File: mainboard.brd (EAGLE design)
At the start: 65 x 56 mm, 19 parts, among them J1 RASPBERRYPI-40-PIN-GPIO

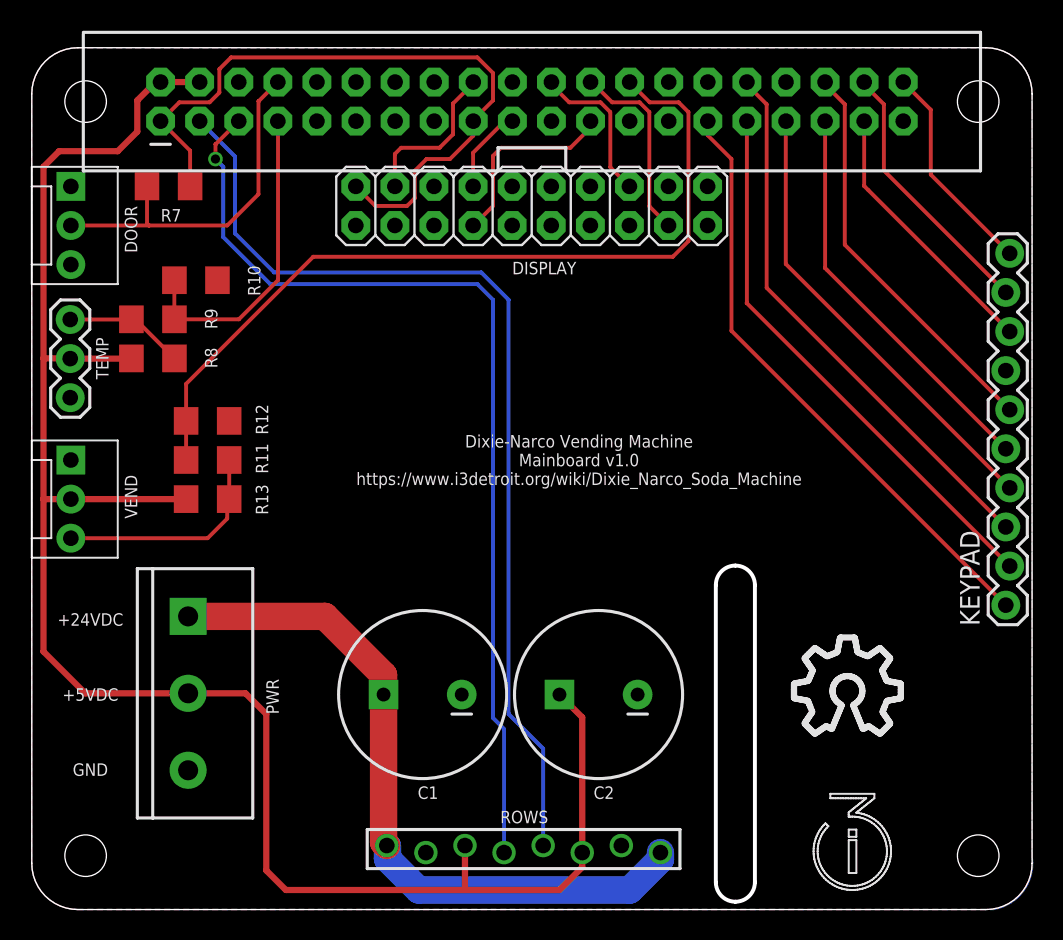
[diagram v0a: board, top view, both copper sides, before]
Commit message: Completed mainboard design edits; buffers for keypad, reworked 5V feed.
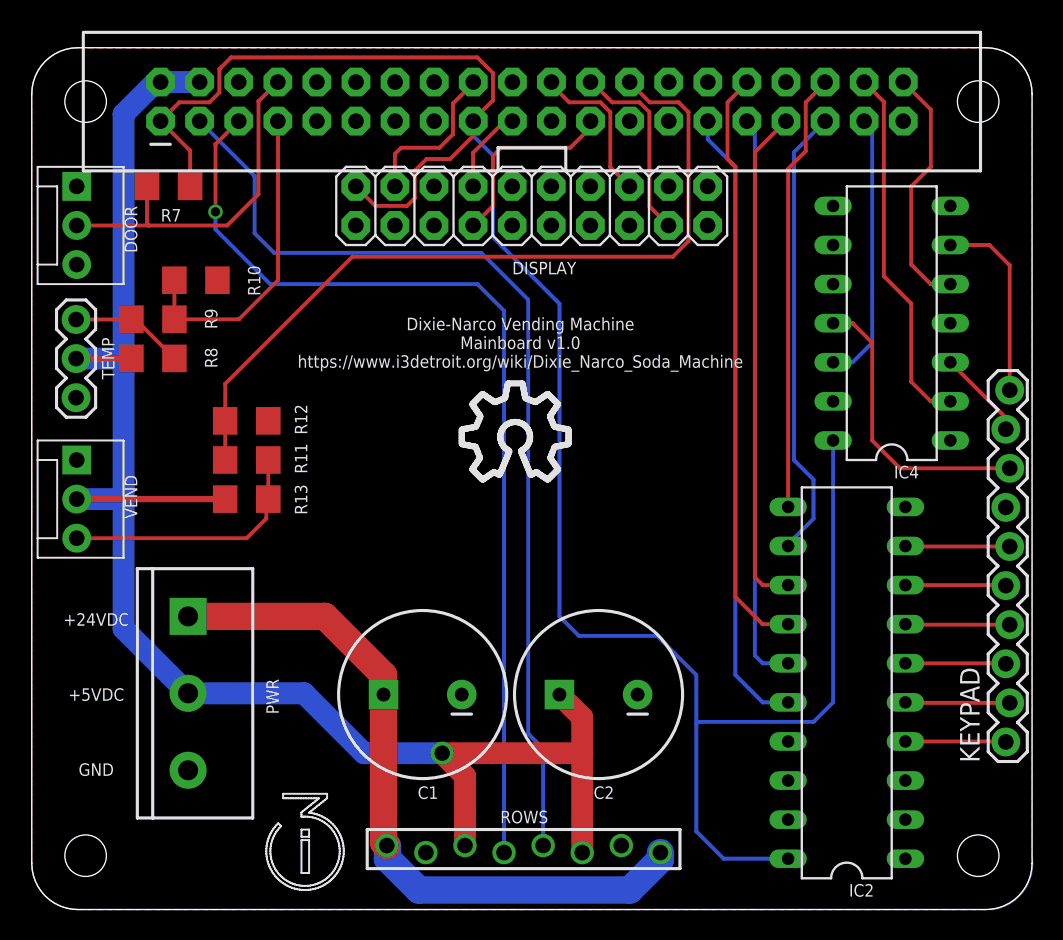
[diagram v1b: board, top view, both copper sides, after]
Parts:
- added IC2: 74HC541N, 74xx-eu:DIL20
- added IC4: 74HC125N, 74xx-eu:DIL14
- moved U$1 35.6 mm to (15.2, 1.27)
- moved U$2 27.2 mm to (27.9, 27.9)
- moved KEYPAD 8.89 mm to (63.4, 10.9)
- moved R11 2.54 mm to (14.0, 29.2)
- moved R12 2.54 mm to (14.0, 31.8)
- moved R13 2.54 mm to (14.0, 26.7)
- moved DOOR 0.38 mm to (2.92, 47.0)
- moved TEMP 0.38 mm to (2.88, 33.3)
- moved VEND_CONFIRM 0.38 mm to (2.92, 29.2)
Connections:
- new net KC1: IC4.6, KEYPAD.10
- new net KC2: IC4.3, KEYPAD.9
- new net KC3: IC4.11, KEYPAD.8
- new net KR1: IC2.4, KEYPAD.1
- new net KR2: IC2.5, KEYPAD.2
- new net KR3: IC2.6, KEYPAD.3
- new net KR4: IC2.7, KEYPAD.4
- new net KR5: IC2.8, KEYPAD.5
- new net KR6: IC2.9, KEYPAD.6
- net +3V3: now also IC2.20, IC4.14
- net GND: now also IC2.1, IC2.10, IC2.19, IC4.1, IC4.13, IC4.4, IC4.7
- net KEYCOL1: now also IC4.5, J1.40; no longer J1.37, KEYPAD.8
- net KEYCOL2: now also IC4.2; no longer KEYPAD.9
- net KEYCOL3: now also IC4.12, J1.37; no longer J1.40, KEYPAD.10
- net KEYROW1: now also IC2.16; no longer KEYPAD.1
- net KEYROW2: now also IC2.15; no longer KEYPAD.2
- net KEYROW3: now also IC2.14; no longer KEYPAD.3
- net KEYROW4: now also IC2.13; no longer KEYPAD.4
- net KEYROW5: now also IC2.12; no longer KEYPAD.5
- net KEYROW6: now also IC2.11; no longer KEYPAD.6
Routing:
- net +3V3: track 45.4 -> 133.7 mm
- net KC3: track 0.00 -> 19.1 mm
- net +5V: track 122.8 -> 109.3 mm, vias 0 -> 1
- net KC1: track 0.00 -> 12.5 mm
- net KR6: track 0.00 -> 6.81 mm
- net KR4: track 0.00 -> 6.81 mm
- net KR2: track 0.00 -> 6.81 mm
- net KR5: track 0.00 -> 6.56 mm
- net KR1: track 0.00 -> 6.56 mm
- net KR3: track 0.00 -> 6.56 mm
- net KEYCOL2: track 17.5 -> 23.8 mm
- net KC2: track 0.00 -> 5.84 mm
- net KEYCOL3: track 14.0 -> 17.7 mm
- net KEYROW5: track 26.2 -> 29.7 mm
- net KEYROW4: track 29.9 -> 32.8 mm
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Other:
- outline, holes or cut-outs redrawn

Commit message: No the one-wire sensor does not need a $0.252 resistor as a pull-up the $0.0254 ones are fine kthxbai.
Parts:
- R8: value 5.1k -> 4.7k
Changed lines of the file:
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@@
 <attribute name="VALUE" x="7.493" y="45.466" size="0.4064" layer="27"/>
 </element>
-<element name="R8" library="SparkFun-Passives" package="1206" value="5.1k" x="7.874" y="35.814" smashed="yes" rot="R180">
+<element name="R8" library="SparkFun-Passives" package="1206" value="4.7k" x="7.874" y="35.814" smashed="yes" rot="R180">
 <attribute name="NAME" x="12.065" y="35.179" size="0.8128" layer="25" rot="R90"/>
 <attribute name="VALUE" x="9.271" y="37.338" size="0.4064" layer="27" rot="R180"/>
